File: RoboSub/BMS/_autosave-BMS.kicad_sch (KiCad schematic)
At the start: 30 parts, among them J1 battery, J2 temp, J3 ExtPwrSw, J4 output, J5 CAN, Q1 PMV28ENEA, SW1 DBG2, SW2 DBG1, SW3 RST, U1 VXO7803, U2 CZ3A07, U5 PCC

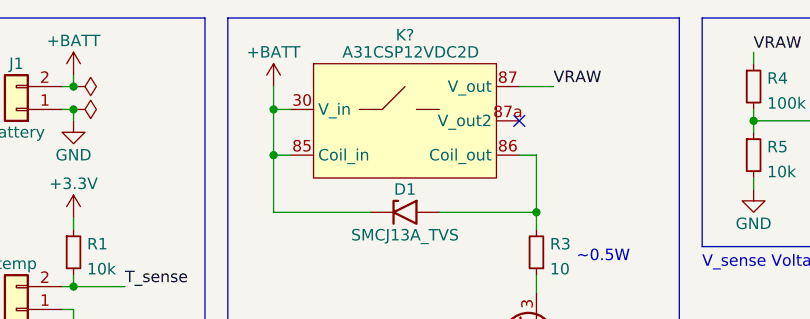
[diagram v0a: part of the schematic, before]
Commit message: updated relay footprint and symbol
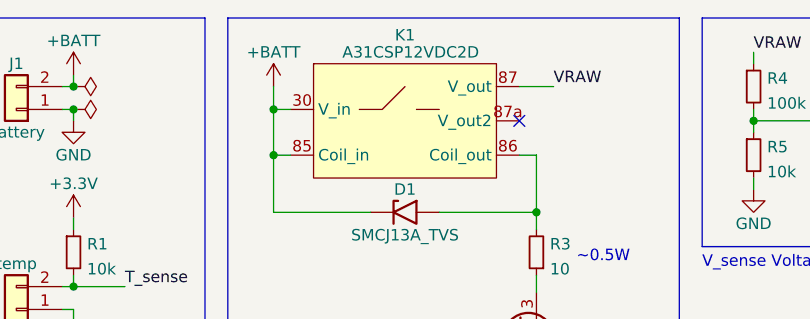
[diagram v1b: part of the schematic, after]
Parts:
- gave numbers to parts that had none: 1
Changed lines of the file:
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@@
   (symbol (lib_id "BMS_Library:A31CSP12VDC2D") (at 113.03 35.56 0) (unit 1)
     (in_bom yes) (on_board yes)
-    (property "Reference" "K?" (id 0) (at 113.03 28.575 0))
+    (property "Reference" "K1" (id 0) (at 113.03 28.575 0))
     (property "Value" "A31CSP12VDC2D" (id 1) (at 113.665 30.48 0))
     (property "Footprint" "BMS_Library:A3_Relay" (id 2) (at 113.03 35.56 0)
@@
     )
     (path "/25ee2213-f0fe-4c7d-ac11-be4f26ffce69"
-      (reference "K?") (unit 1) (value "A31CSP12VDC2D") (footprint "BMS_Library:A3_Relay")
+      (reference "K1") (unit 1) (value "A31CSP12VDC2D") (footprint "BMS_Library:A3_Relay")
     )
     (path "/96040761-b0e5-47a9-8ba7-7d9622476861"
